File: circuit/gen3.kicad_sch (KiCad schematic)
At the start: 10 parts, among them J1 Jack-DC, J2 Conn_02x20_Row_Letter_Last, J3 Conn_02x20_Row_Letter_Last, J4 Conn_01x02_Socket, SW1 SW_Wuerth_450301014042

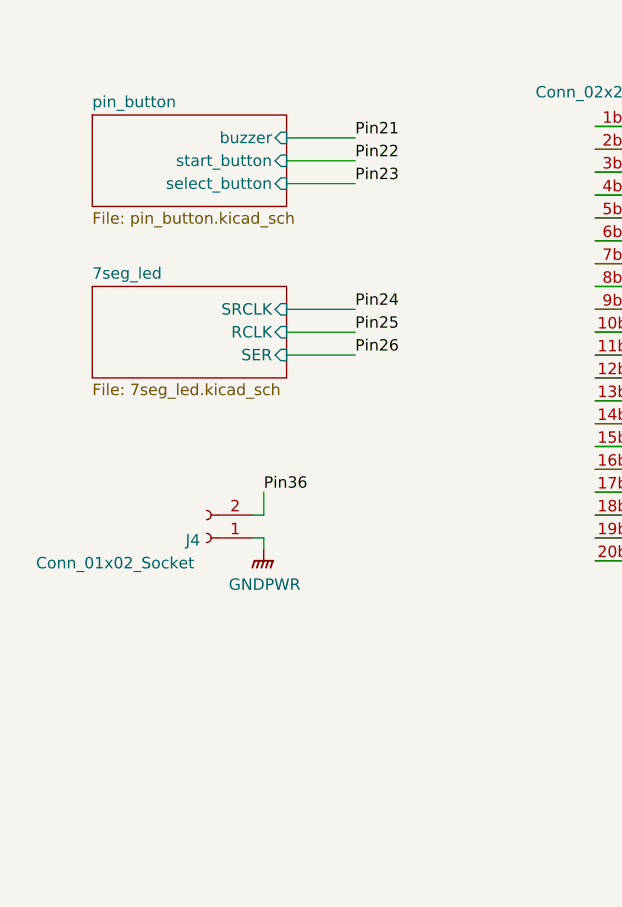
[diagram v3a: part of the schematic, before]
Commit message: [add] add connector for detonator
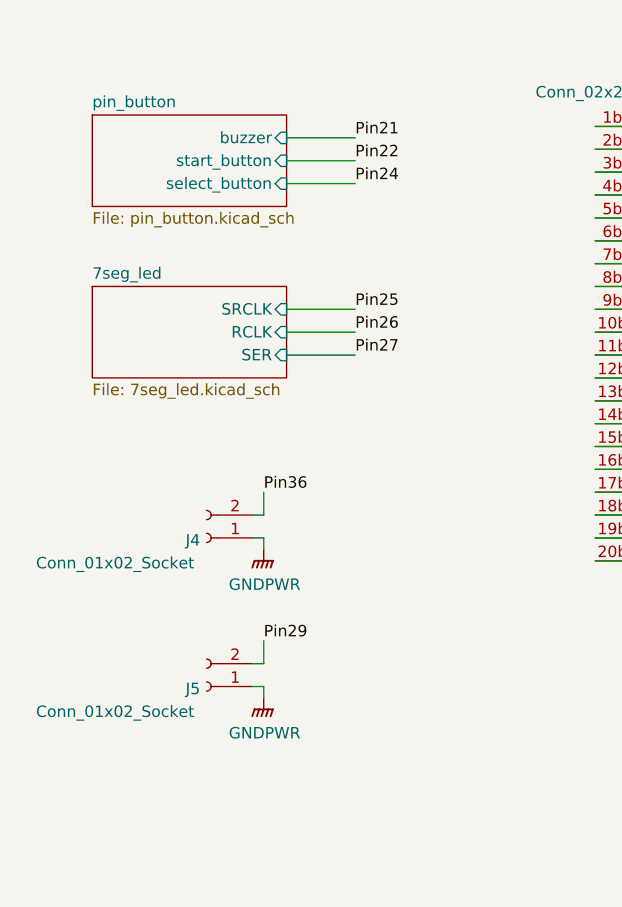
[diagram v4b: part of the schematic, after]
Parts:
- added J5: Conn_01x02_Socket, Connector_JST:JST_XH_S2B-XH-A_1x02_P2.50mm_Horizontal, symbol Connector:Conn_01x02_Socket
- H1, H2, H3, H4: footprint (none) -> MountingHole:MountingHole_2.7mm_M2.5
- SW1: footprint Button_Switch_THT:SW_Slide-03_Wuerth-WS-SLTV_10x2.5x6.4_P2.54mm -> Button_Switch_THT:SW_Slide_SPDT_Straight_CK_OS102011MS2Q
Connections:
- net GNDPWR: now also J5.1 (Pin_1)
- net Pin29: now also J5.2 (Pin_2)
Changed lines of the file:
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@@
+	(wire
+		(pts
+			(xy 73.66 130.81) (xy 72.39 130.81)
+		)
+		(stroke
+			(width 0)
+			(type default)
+		)
+	)
 	(wire
 		(pts
@@
 	(wire
 		(pts
+			(xy 72.39 133.35) (xy 73.66 133.35)
+		)
+		(stroke
+			(width 0)
+			(type default)
+		)
+	)
+	(wire
+		(pts
 			(xy 110.49 71.12) (xy 123.19 71.12)
 		)
@@
 	(wire
 		(pts
+			(xy 73.66 128.27) (xy 73.66 130.81)
+		)
+		(stroke
+			(width 0)
+			(type default)
+		)
+	)
+	(wire
+		(pts
 			(xy 110.49 78.74) (xy 123.19 78.74)
 		)
@@
 		(pts
 			(xy 209.55 113.03) (xy 222.25 113.03)
+		)
+		(stroke
+			(width 0)
+			(type default)
+		)
+	)
+	(wire
+		(pts
+			(xy 73.66 133.35) (xy 73.66 134.62)
 		)
 		(stroke
@@
 		)
 	)
-	(label "Pin23"
+	(label "Pin24"
 		(at 83.82 77.47 0)
 		(effects
@@
 		)
 	)
+	(label "Pin29"
+		(at 73.66 128.27 0)
+		(effects
+			(font
+				(size 1.27 1.27)
+			)
+			(justify left bottom)
+		)
+	)
 	(label "Pin22"
 		(at 209.55 77.47 180)
@@
 		)
 	)
-	(label "Pin24"
+	(label "Pin25"
 		(at 83.82 91.44 0)
 		(effects
@@
 		)
 	)
-	(label "Pin26"
+	(label "Pin27"
 		(at 83.82 96.52 0)
 		(effects
@@
 		)
 	)
-	(label "Pin25"
+	(label "Pin26"
 		(at 83.82 93.98 0)
 		(effects
@@
 			)
 		)
-		(property "Footprint" ""
+		(property "Footprint" "MountingHole:MountingHole_2.7mm_M2.5"
 			(at 48.26 163.83 0)
 			(effects
@@
 			)
 		)
-		(property "Footprint" ""
+		(property "Footprint" "MountingHole:MountingHole_2.7mm_M2.5"
 			(at 48.26 173.99 0)
 			(effects
@@
 				(path "/4fc99a72-ed0b-4d28-88d8-569af68d8cfc"
 					(reference "H3")
+					(unit 1)
+				)
+			)
+		)
+	)
+	(symbol
+		(lib_id "power:GNDPWR")
+		(at 73.66 134.62 0)
+		(unit 1)
+		(exclude_from_sim no)
+		(in_bom yes)
+		(on_board yes)
+		(dnp no)
+		(property "Reference" "#PWR02"
+			(at 73.66 139.7 0)
+			(effects
+				(font
+					(size 1.27 1.27)
+				)
+				(hide yes)
+			)
+		)
+		(property "Value" "GNDPWR"
+			(at 73.7616 138.5316 0)
+			(effects
+				(font
+					(size 1.27 1.27)
+				)
+			)
+		)
+		(property "Footprint" ""
+			(at 73.66 135.89 0)
+			(effects
+				(font
+					(size 1.27 1.27)
+				)
+				(hide yes)
+			)
+		)
+		(property "Datasheet" ""
+			(at 73.66 135.89 0)
+			(effects
+				(font
+					(size 1.27 1.27)
+				)
+				(hide yes)
+			)
+		)
+		(property "Description" ""
+			(at 73.66 134.62 0)
+			(effects
+				(font
+					(size 1.27 1.27)
+				)
+				(hide yes)
+			)
+		)
+		(pin "1"
+		)
+		(instances
+			(project "gen3"
+				(path "/4fc99a72-ed0b-4d28-88d8-569af68d8cfc"
+					(reference "#PWR02")
 					(unit 1)
 				)
@@
 			)
 		)
-		(property "Footprint" ""
+		(property "Footprint" "MountingHole:MountingHole_2.7mm_M2.5"
 			(at 72.39 163.83 0)
 			(effects
@@
 	)
 	(symbol
+		(lib_id "Connector:Conn_01x02_Socket")
+		(at 67.31 133.35 180)
+		(unit 1)
+		(exclude_from_sim no)
+		(in_bom yes)
+		(on_board yes)
+		(dnp no)
+		(property "Reference" "J5"
+			(at 65.786 133.604 0)
+			(effects
+				(font
+					(size 1.27 1.27)
+				)
+			)
+		)
+		(property "Value" "Conn_01x02_Socket"
+			(at 57.15 136.144 0)
+			(effects
+				(font
+					(size 1.27 1.27)
+				)
+			)
+		)
+		(property "Footprint" "Connector_JST:JST_XH_S2B-XH-A_1x02_P2.50mm_Horizontal"
+			(at 67.31 133.35 0)
+			(effects
+				(font
+					(size 1.27 1.27)
+				)
+				(hide yes)
+			)
+		)
+		(property "Datasheet" "~"
+			(at 67.31 133.35 0)
+			(effects
+				(font
+					(size 1.27 1.27)
+				)
+				(hide yes)
+			)
+		)
+		(property "Description" ""
+			(at 67.31 133.35 0)
+			(effects
+				(font
+					(size 1.27 1.27)
+				)
+				(hide yes)
+			)
+		)
+		(pin "1"
+		)
+		(pin "2"
+		)
+		(instances
+			(project "gen3"
+				(path "/4fc99a72-ed0b-4d28-88d8-569af68d8cfc"
+					(reference "J5")
+					(unit 1)
+				)
+			)
+		)
+	)
+	(symbol
 		(lib_id "Switch:SW_Wuerth_450301014042")
 		(at 161.29 39.37 270)
@@
 			)
 		)
-		(property "Footprint" "Button_Switch_THT:SW_Slide-03_Wuerth-WS-SLTV_10x2.5x6.4_P2.54mm"
+		(property "Footprint" "Button_Switch_THT:SW_Slide_SPDT_Straight_CK_OS102011MS2Q"
 			(at 151.13 39.37 0)
 			(effects
@@
 			)
 		)
-		(property "Footprint" ""
+		(property "Footprint" "MountingHole:MountingHole_2.7mm_M2.5"
 			(at 72.39 173.99 0)
 			(effects

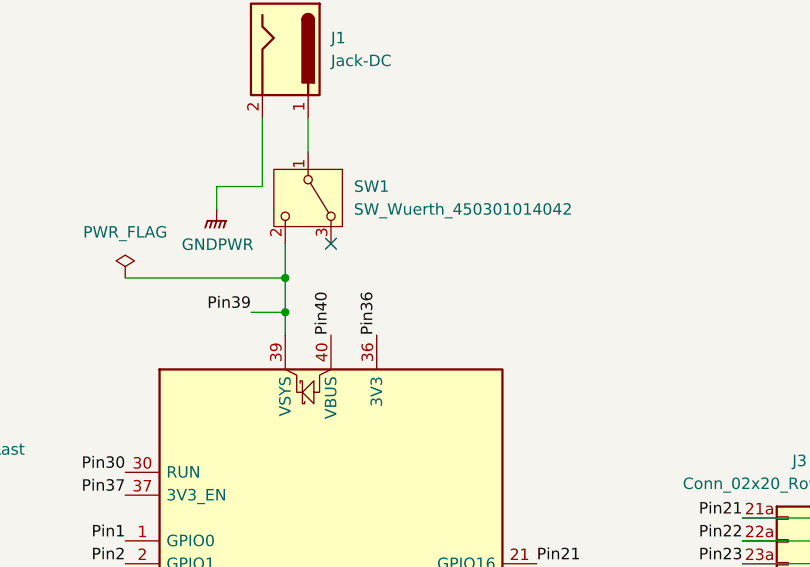
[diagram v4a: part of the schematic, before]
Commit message: [!][fix] fix routing 3v3 signal
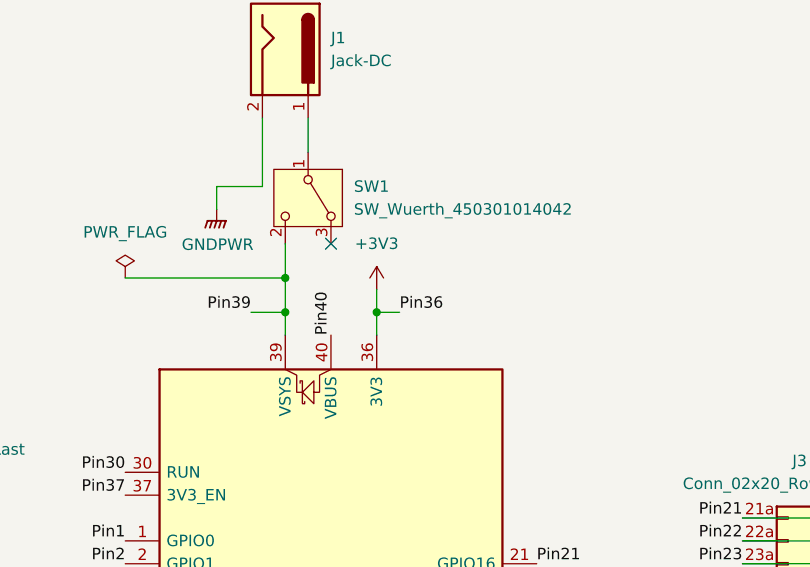
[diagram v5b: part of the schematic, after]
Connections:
- net Pin36 renamed +3V3
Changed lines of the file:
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@@
+	)
+	(junction
+		(at 168.91 52.07)
+		(diameter 0)
+		(color 0 0 0 0)
 	)
 	(junction
@@
 	(wire
 		(pts
+			(xy 171.45 52.07) (xy 168.91 52.07)
+		)
+		(stroke
+			(width 0)
+			(type default)
+		)
+	)
+	(wire
+		(pts
 			(xy 76.2 72.39) (xy 83.82 72.39)
 		)
@@
 	(wire
 		(pts
+			(xy 168.91 52.07) (xy 168.91 54.61)
+		)
+		(stroke
+			(width 0)
+			(type default)
+		)
+	)
+	(wire
+		(pts
 			(xy 209.55 97.79) (xy 222.25 97.79)
 		)
@@
 		(pts
 			(xy 110.49 114.3) (xy 123.19 114.3)
+		)
+		(stroke
+			(width 0)
+			(type default)
+		)
+	)
+	(wire
+		(pts
+			(xy 168.91 49.53) (xy 168.91 52.07)
 		)
 		(stroke
@@
 	)
 	(label "Pin36"
-		(at 168.91 54.61 90)
+		(at 171.45 52.07 0)
 		(effects
 			(font
@@
 					(unit 1)
 				)
+			)
+		)
+	)
+	(symbol
+		(lib_id "power:+3V3")
+		(at 168.91 49.53 0)
+		(unit 1)
+		(exclude_from_sim no)
+		(in_bom yes)
+		(on_board yes)
+		(dnp no)
+		(fields_autoplaced yes)
+		(property "Reference" "#PWR024"
+			(at 168.91 53.34 0)
+			(effects
+				(font
+					(size 1.27 1.27)
+				)
+				(hide yes)
+			)
+		)
+		(property "Value" "+3V3"
+			(at 168.91 44.45 0)
+			(effects
+				(font
+					(size 1.27 1.27)
+				)
+			)
+		)
+		(property "Footprint" ""
+			(at 168.91 49.53 0)
+			(effects
+				(font
+					(size 1.27 1.27)
+				)
+				(hide yes)
+			)
+		)
+		(property "Datasheet" ""
+			(at 168.91 49.53 0)
+			(effects
+				(font
+					(size 1.27 1.27)
+				)
+				(hide yes)
+			)
+		)
+		(property "Description" "Power symbol creates a global label with name \"+3V3\""
+			(at 168.91 49.53 0)
+			(effects
+				(font
+					(size 1.27 1.27)
+				)
+				(hide yes)
+			)
+		)
+		(pin "1"
+		)
+		(instances
+			(project ""
+				(path "/4fc99a72-ed0b-4d28-88d8-569af68d8cfc"
+					(reference "#PWR024")
+					(unit 1)
+				)
